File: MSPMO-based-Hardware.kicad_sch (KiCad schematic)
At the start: 22 parts, among them J1 Conn_ARM_SWD_TagConnect_TC2030, J2 USB_C_Receptacle_USB2.0_16P, U1 MSPMOG3507SPTR, U2 USBLC6-2SC6, U3 SPX3819M5-L-3-3, X1 8MHz

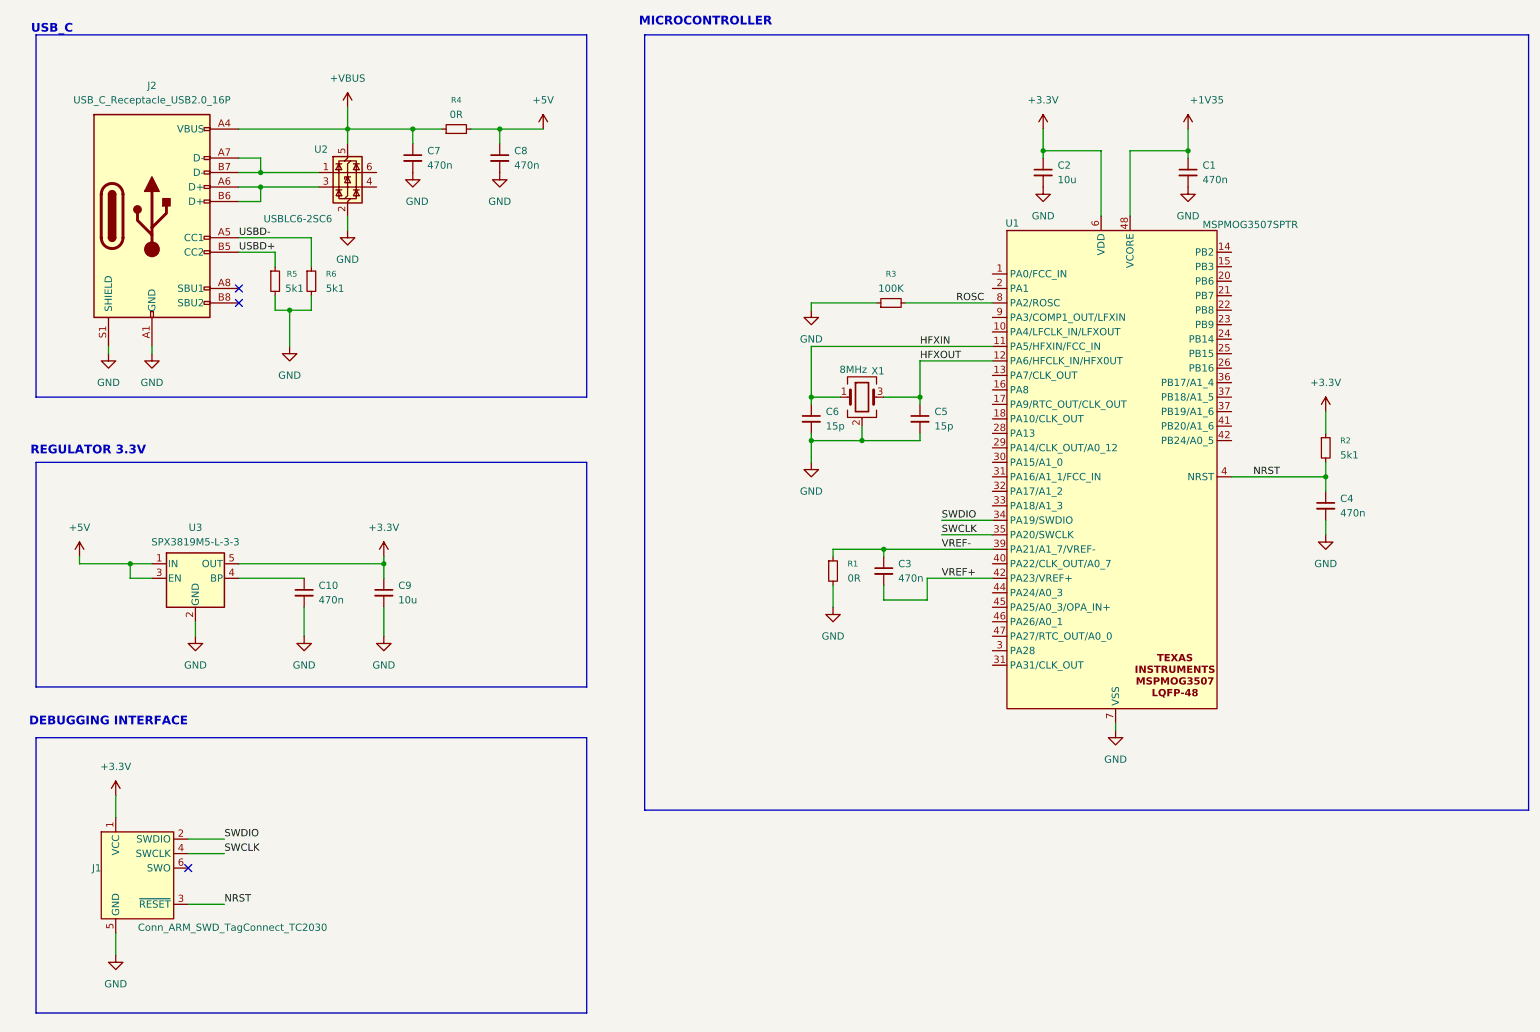
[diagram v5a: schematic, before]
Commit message: feat(hardware): add net class configurations and relax ERC settings
Configure net class patterns for USB, UART, and I2C protocols with designated colors and wire widths. Add CH340E and SENSOR-LIS2DH sheets to the design hierarchy. Relax ERC constraints by changing pin connection warnings to ignore.
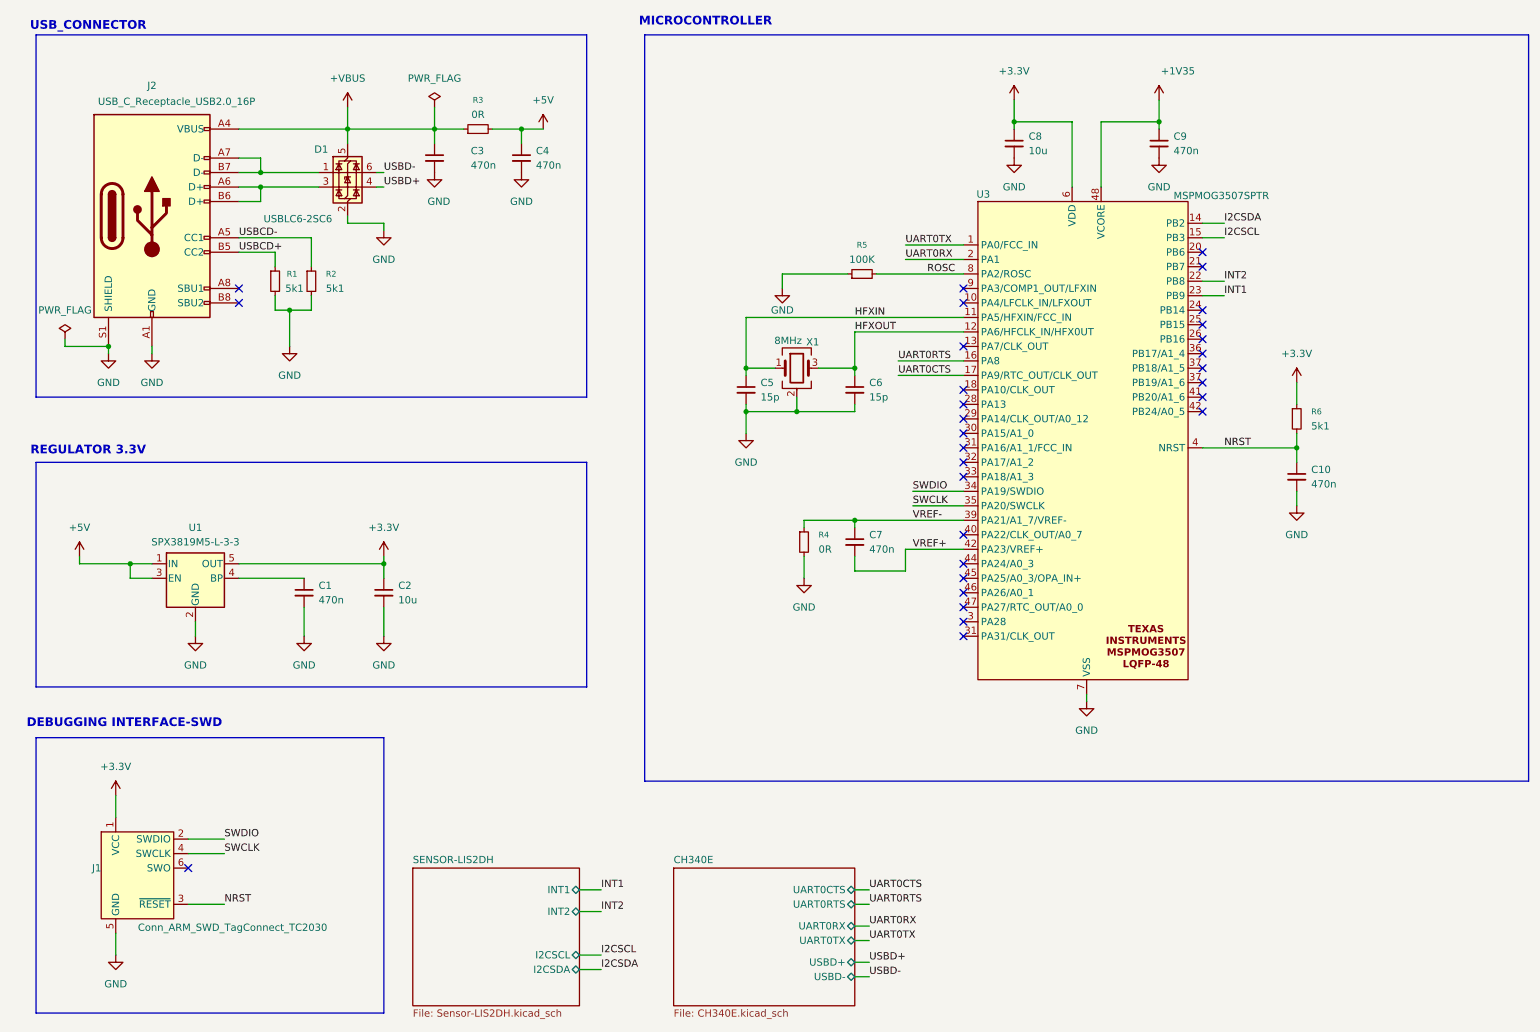
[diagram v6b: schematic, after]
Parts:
- renumbered C10 to C1, C4 to C10, C9 to C2, C7 to C3, C8 to C4, C6 to C5, C5 to C6, C3 to C7, C2 to C8, C1 to C9, U2 to D1, R5 to R1, R6 to R2, R4 to R3, R1 to R4, R3 to R5, R2 to R6, U3 to U1, U1 to U3
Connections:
- net USBD+: now also D1.4 (I/O2); no longer J2.B5 (CC2), R1.1
- net USBD-: now also D1.6 (I/O1); no longer J2.A5 (CC1), R2.1
- net UART0TX: now reaches U3.1 (PA0/FCC_IN)
- net I2CSDA: now reaches U3.14 (PB2)
- net I2CSCL: now reaches U3.15 (PB3)
- net UART0RTS: now reaches U3.16 (PA8)
- net UART0CTS: now reaches U3.17 (PA9/RTC_OUT/CLK_OUT)
- net UART0RX: now reaches U3.2 (PA1)
- net INT2: now reaches U3.22 (PB8)
- net INT1: now reaches U3.23 (PB9)
- new net USBCD+: J2.B5 (CC2), R1.1
- new net USBCD-: J2.A5 (CC1), R2.1
- no-connect marks 3 -> 30
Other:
- added sheet CH340E (CH340E.kicad_sch)
- added sheet SENSOR-LIS2DH (Sensor-LIS2DH.kicad_sch)
- note added: "DEBUGGING INTERFACE-SWD"
- note added: "USB_CONNECTOR"
- note removed: "DEBUGGING INTERFACE"
- note removed: "USB_C"
- moved on the sheet: C10, C3, C4, C5, C6, C7, C8, C9, R3, R4, R5, R6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

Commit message: feat(hardware): add fiducial markers and mounting holes to PCB schematic
Add manufacturing aids to the KiCad schematic including:
- Three fiducial markers (FID1, FID2, FID3) for SMT alignment during assembly
- Four M3 mounting holes with connected pads (MH1-MH4) for secure PCB mounting
- Associated GND connections and text labels for documentation
- Also adds KLC compliance properties to various schematic components
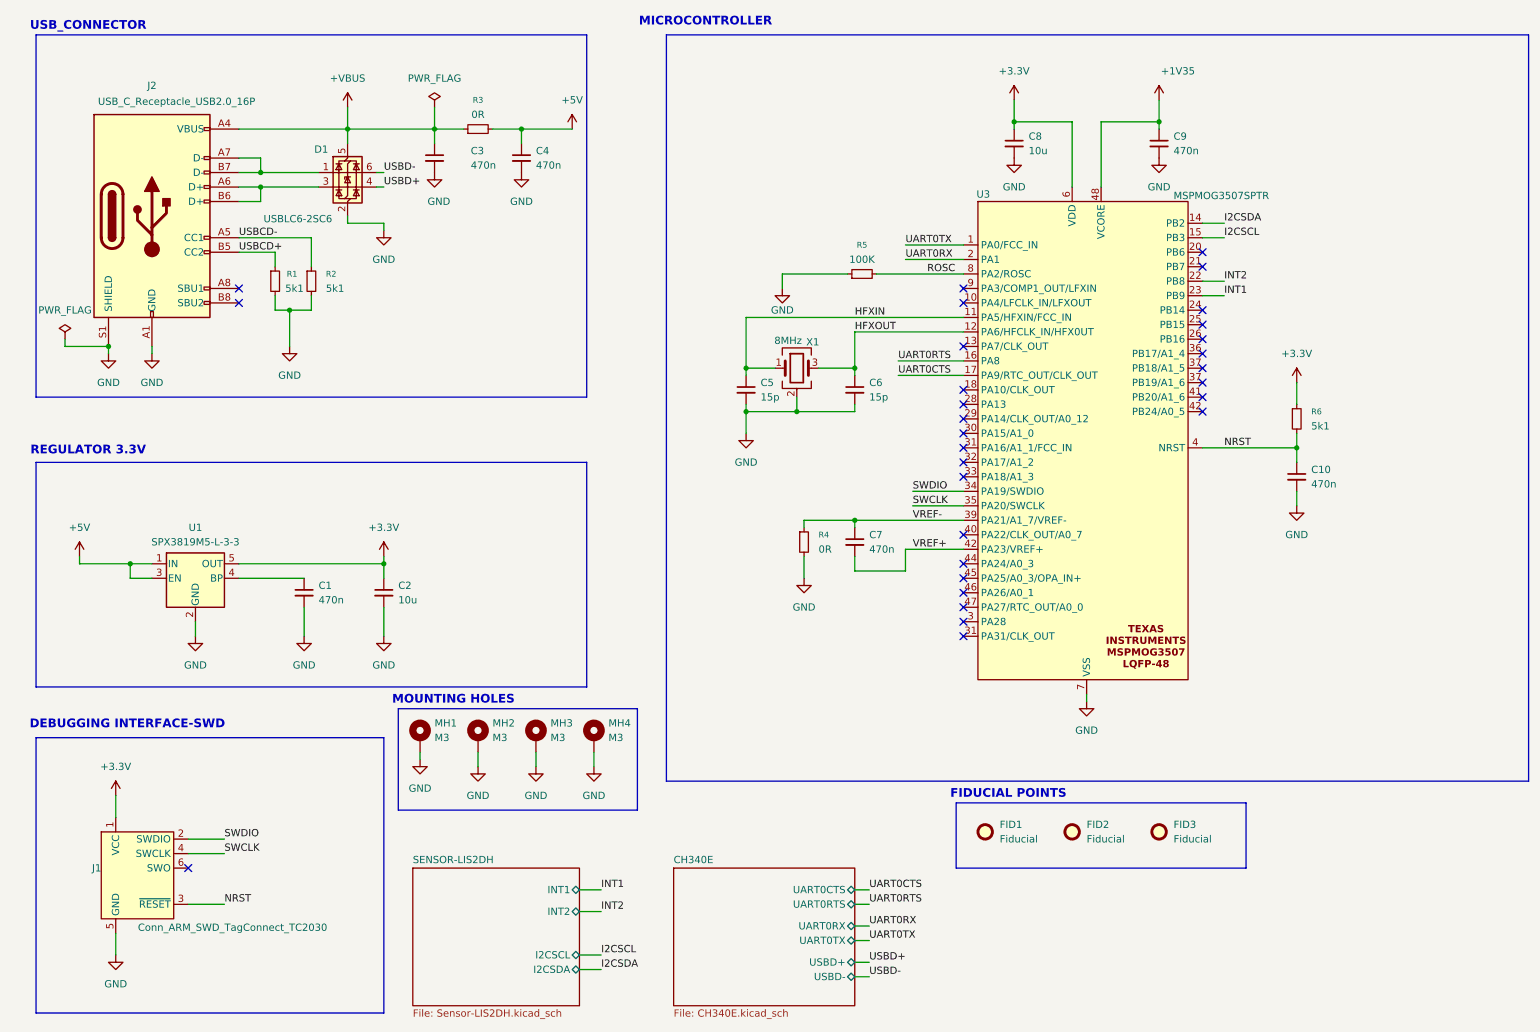
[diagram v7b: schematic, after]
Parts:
- added FID1, FID2, FID3: Fiducial, Fiducial:Fiducial_1mm_Mask2mm, symbol Mechanical:Fiducial
- added MH1, MH2, MH3, MH4: M3, MountingHole:MountingHole_2.7mm_M2.5_Pad_Via, symbol Mechanical:MountingHole_Pad
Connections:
- net GND: now also MH1.1, MH2.1, MH3.1, MH4.1
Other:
- note added: "FIDUCIAL POINTS"
- note added: "MOUNTING HOLES"

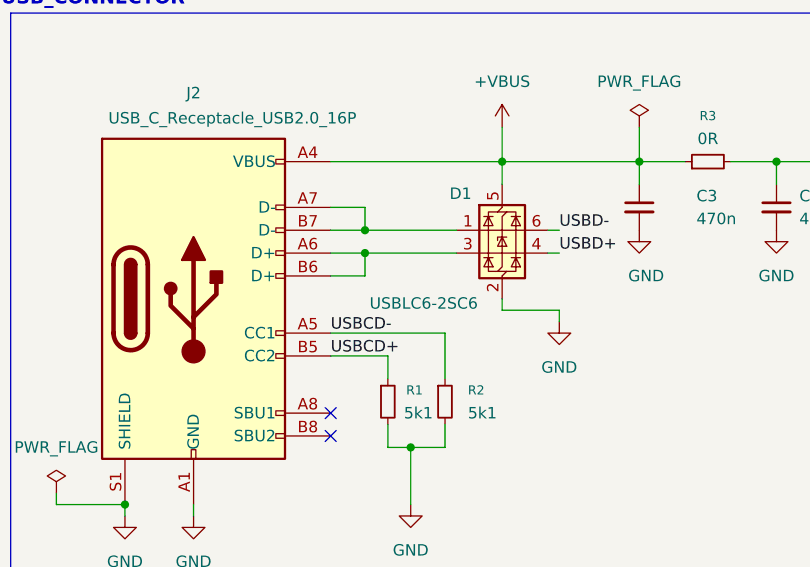
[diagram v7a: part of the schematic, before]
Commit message: fix(hardware): reposition USB CDC differential signal labels in schematic
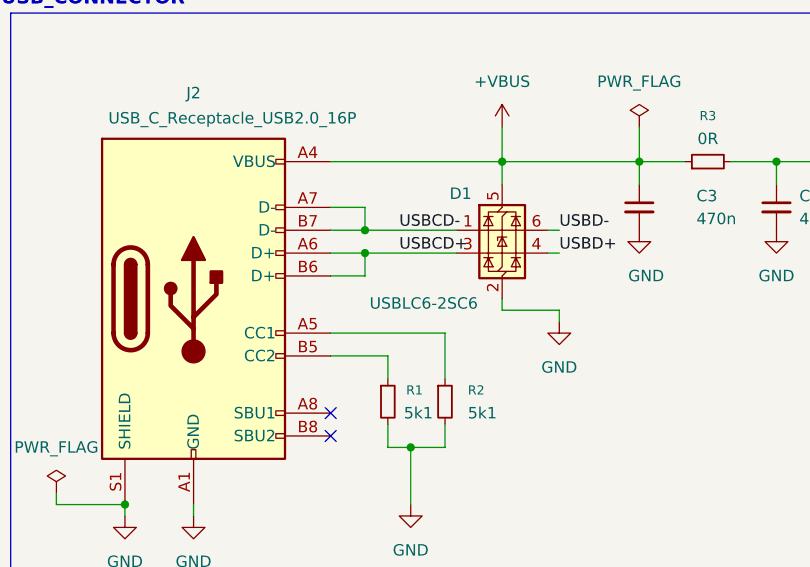
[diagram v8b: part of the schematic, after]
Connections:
- net USBCD+: now also D1.3 (I/O2), J2.A6 (D+), J2.B6 (D+); no longer J2.B5 (CC2), R1.1
- net USBCD-: now also D1.1 (I/O1), J2.A7 (D-), J2.B7 (D-); no longer J2.A5 (CC1), R2.1
- new net: J2.A5 (CC1), R2.1
- new net: J2.B5 (CC2), R1.1
